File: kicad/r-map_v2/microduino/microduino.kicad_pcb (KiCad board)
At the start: 2 copper layers, 25.4 x 29.2 mm, 15 parts, among them P1 CONN_01X02, P2 CONN_RELE_BOARD, P3 CONN_01X05, P4 CONFIG, P5 USB, U1 Microduino, U2 ESDA6V1-5SC6, U3 LP2985LV, U4 TMP275

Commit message: Add files from last commit on sourceforge
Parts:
- removed R1: 1K0, w_smd_resistors:r_1206
- D1: value LED -> LED_SMD
- P5: value USB -> USB_OTG
- R2: value R -> 150
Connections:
- net Net-(C1-Pad1) renamed /+5V
- net Net-(C3-Pad1) renamed /+3.3V
- net Net-(P3-Pad2) renamed /SCL
- net Net-(P3-Pad3) renamed /SDA
- U4 pad 5: Net-(R1-Pad1) -> GND
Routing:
- net GND: track 93.1 -> 105.6 mm
- net Net-(R1-Pad1): track 11.2 -> 0.00 mm
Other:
- board text added: "+5V"
- board text added: "-"
- board text added: "3.3V"
- board text added: "GND"
- board text added: "REL1"
- board text added: "REL2"
- board text added: "REL3"
- board text added: "REL4"
- board text added: "SCL"
- board text added: "SDA"
- board text added: "SET"

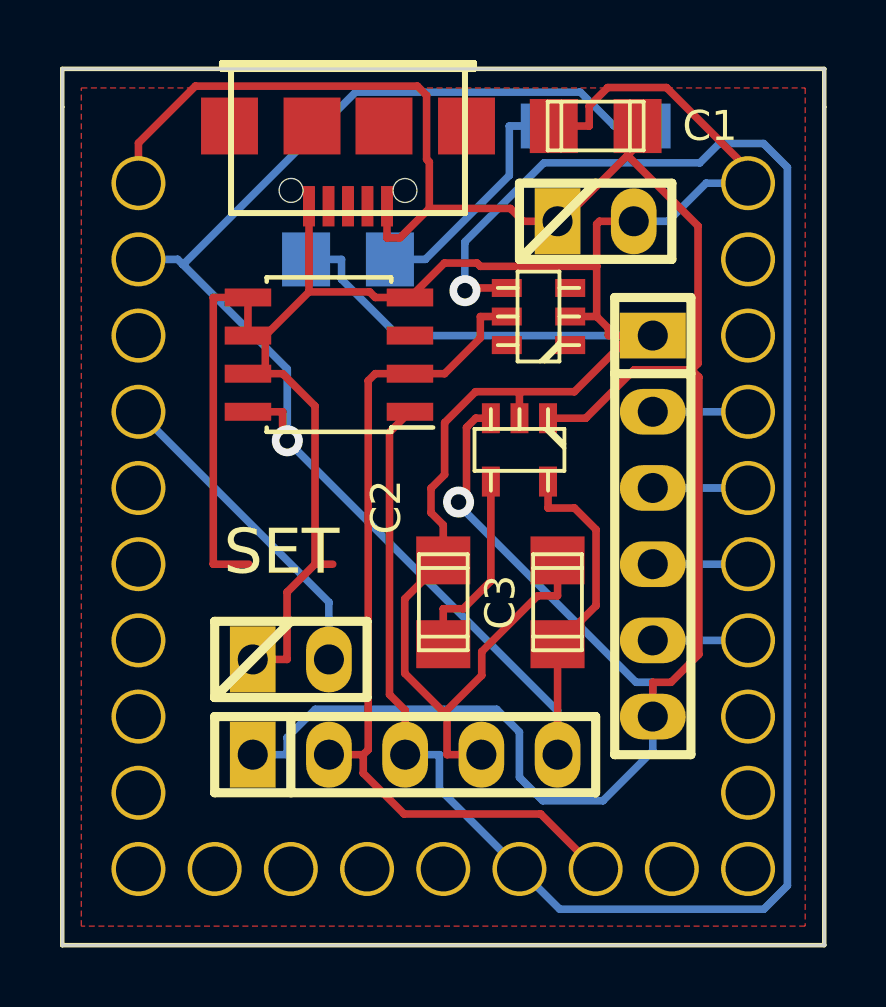
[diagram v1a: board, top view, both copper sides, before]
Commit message: Modifiche a schema elettrico su modulo bluethoot, modificate connessioni per seriale 1. Modulo stima-i2c modificati pin per rele' e aggiunte connessioni esd su alimentazione. Rigenerati pcb.
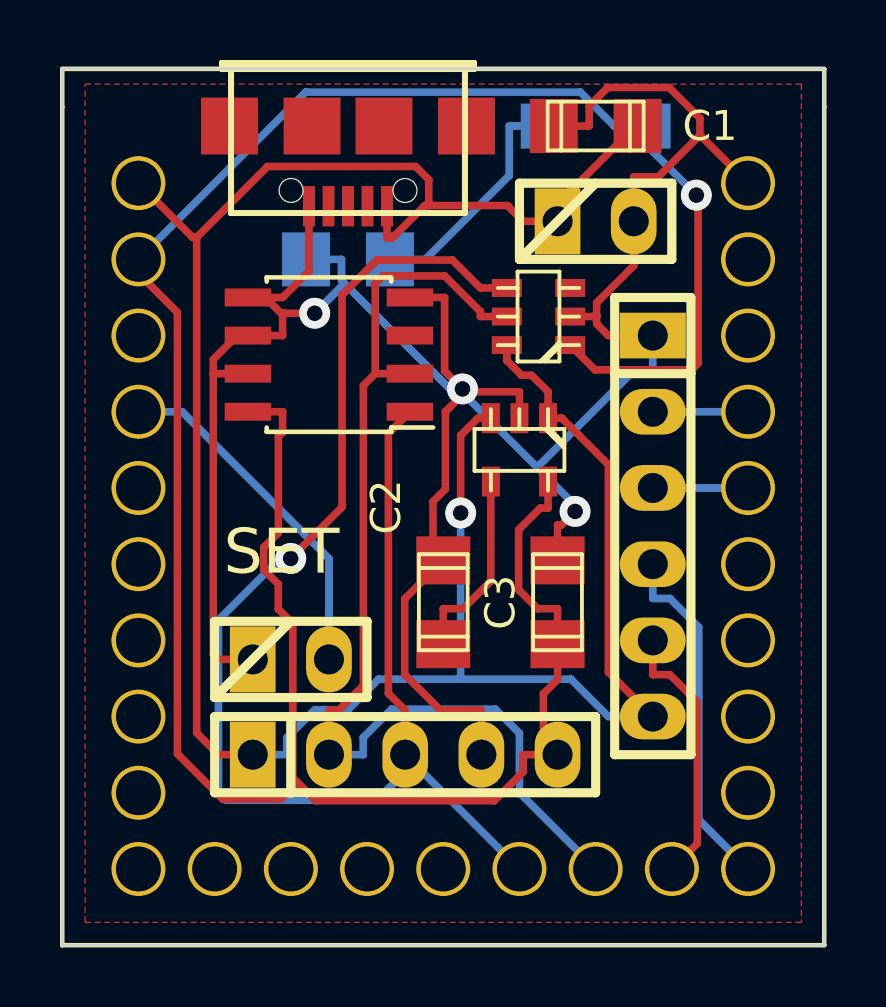
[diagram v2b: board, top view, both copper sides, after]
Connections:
- P5 pad 2: (no net) -> Net-(P5-Pad2)
- P5 pad 3: (no net) -> Net-(P5-Pad3)
- P5 pad 4: (no net) -> Net-(P5-Pad4)
- U1 pad 10: (no net) -> Net-(P2-Pad4)
- U1 pad 11: (no net) -> Net-(P2-Pad5)
- U1 pad 14: (no net) -> Net-(U1-Pad14)
- U1 pad 15: (no net) -> Net-(U1-Pad15)
- U1 pad 16: (no net) -> Net-(U1-Pad16)
- U1 pad 17: (no net) -> Net-(U1-Pad17)
- U1 pad 18: (no net) -> Net-(U1-Pad18)
- U1 pad 19: (no net) -> Net-(U1-Pad19)
- U1 pad 2: (no net) -> Net-(U1-Pad2)
- U1 pad 20: (no net) -> Net-(U1-Pad20)
- U1 pad 21: (no net) -> Net-(U1-Pad21)
- U1 pad 22: (no net) -> Net-(U1-Pad22)
- U1 pad 23: (no net) -> Net-(U1-Pad23)
- U1 pad 25: (no net) -> Net-(U1-Pad25)
- U1 pad 3: (no net) -> Net-(U1-Pad3)
- U1 pad 6: Net-(P2-Pad4) -> Net-(U1-Pad6)
- U1 pad 7: Net-(P2-Pad5) -> Net-(U1-Pad7)
- U1 pad 8: (no net) -> Net-(U1-Pad8)
- U1 pad 9: (no net) -> Net-(U1-Pad9)
- U2 pad 1: (no net) -> /+3.3V
- U2 pad 3: (no net) -> Net-(U2-Pad3)
- U2 pad 6: (no net) -> /+5V
- U4 pad 3: (no net) -> Net-(U4-Pad3)
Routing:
- net /+3.3V: track 54.4 -> 90.1 mm
- net GND: track 105.6 -> 87.4 mm, vias 0 -> 3
- net /SDA: track 67.2 -> 49.3 mm
- net Net-(P2-Pad4): track 3.18 -> 11.8 mm
- net /SCL: track 29.3 -> 36.1 mm
- net Net-(P2-Pad5): track 3.18 -> 8.92 mm
- net /+5V: track 85.6 -> 82.6 mm
- net Net-(P4-Pad2): track 10.9 -> 11.7 mm

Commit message: Aggiunto ponticello a saldare per uscita 3.3V. Nuovo design per i2chub
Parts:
- added P6: CONN_01X01, Measurement_Points:Measurement_Point_Square-SMD-Pad_Small, B.Cu at (144.8, 104.1)
- added P7: CONN_01X01, Measurement_Points:Measurement_Point_Square-SMD-Pad_Small, B.Cu at (142.2, 104.1)
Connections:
- U3 pad 5: /+3.3V -> Net-(P6-Pad1)
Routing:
- net /+3.3V: track 90.1 -> 62.2 mm, vias 1 -> 2
- net /SDA: track 49.3 -> 24.0 mm, vias 1 -> 0
- net /SCL: track 36.1 -> 47.3 mm, vias 0 -> 1
- net /+5V: track 82.6 -> 93.3 mm
- net Net-(P6-Pad1): track 0.00 -> 8.43 mm, vias 0 -> 1
- net GND: track 87.4 -> 88.7 mm, vias 3 -> 1

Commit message: Sistemato orientamento case led smd, generati files gbr per i2c hub e breakout board
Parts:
- turned D1 to 180 degrees
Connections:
- D1 pad 1: Net-(D1-Pad1) -> /+3.3V
- D1 pad 2: /+3.3V -> Net-(D1-Pad2)
- P5 pad 2: Net-(P5-Pad2) -> (no net)
- P5 pad 3: Net-(P5-Pad3) -> (no net)
- P5 pad 4: Net-(P5-Pad4) -> (no net)
- R2 pad 1: Net-(D1-Pad1) -> Net-(D1-Pad2)
- U1 pad 14: Net-(U1-Pad14) -> (no net)
- U1 pad 15: Net-(U1-Pad15) -> (no net)
- U1 pad 16: Net-(U1-Pad16) -> (no net)
- U1 pad 17: Net-(U1-Pad17) -> (no net)
- U1 pad 18: Net-(U1-Pad18) -> (no net)
- U1 pad 19: Net-(U1-Pad19) -> (no net)
- U1 pad 2: Net-(U1-Pad2) -> (no net)
- U1 pad 20: Net-(U1-Pad20) -> (no net)
- U1 pad 21: Net-(U1-Pad21) -> (no net)
- U1 pad 22: Net-(U1-Pad22) -> (no net)
- U1 pad 23: Net-(U1-Pad23) -> (no net)
- U1 pad 25: Net-(U1-Pad25) -> (no net)
- U1 pad 3: Net-(U1-Pad3) -> (no net)
- U1 pad 6: Net-(U1-Pad6) -> (no net)
- U1 pad 7: Net-(U1-Pad7) -> (no net)
- U1 pad 8: Net-(U1-Pad8) -> (no net)
- U1 pad 9: Net-(U1-Pad9) -> (no net)
- U2 pad 3: Net-(U2-Pad3) -> (no net)
- U4 pad 3: Net-(U4-Pad3) -> (no net)
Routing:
- net Net-(D1-Pad2): track 0.00 -> 7.92 mm
- net Net-(D1-Pad1): track 7.92 -> 0.00 mm

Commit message: Aggiornamento lista componenti e cancellazione vecchi files
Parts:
- U3: value LP2985LV -> REG113NA-3.3/250
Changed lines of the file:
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@@
-(kicad_pcb (version 4) (host pcbnew 0.201509251832+6217~30~ubuntu14.04.1-product)
+(kicad_pcb (version 4) (host pcbnew 0.201510090346+6256~30~ubuntu14.04.1-product)
   (general
     (links 43)
     (no_connects 0)
-    (area 135.560999 88.350089 177.545 118.439001)
+    (area 135.560999 88.350089 161.619001 118.439001)
     (thickness 1.6)
     (drawings 21)
@@
       (effects (font (size 1 1) (thickness 0.2)))
     )
-    (fp_text value LP2985LV (at 0 0 180) (layer F.SilkS) hide
+    (fp_text value REG113NA-3.3/250 (at 0 0 180) (layer F.SilkS) hide
       (effects (font (size 0.50038 0.50038) (thickness 0.09906)))
     )

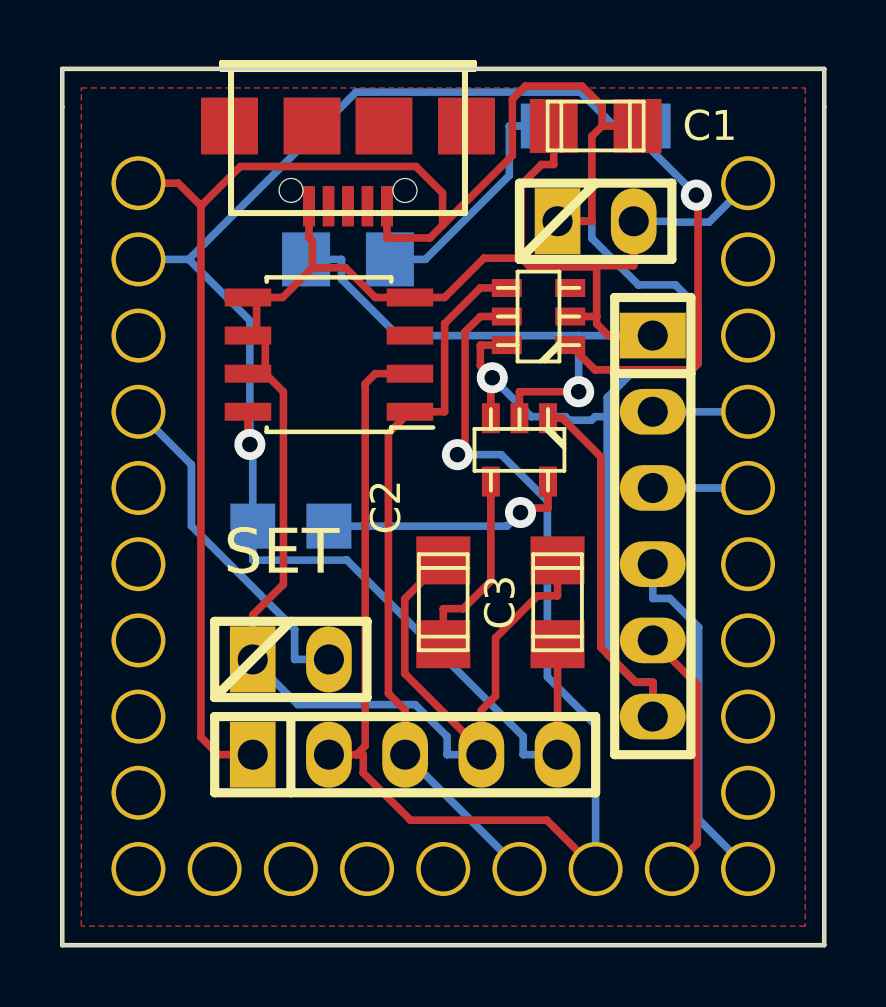
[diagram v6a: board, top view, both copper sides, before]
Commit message: Nouva versione pcb, doppia schermatura, allargamento piste, rimozione connessioni T ed Y
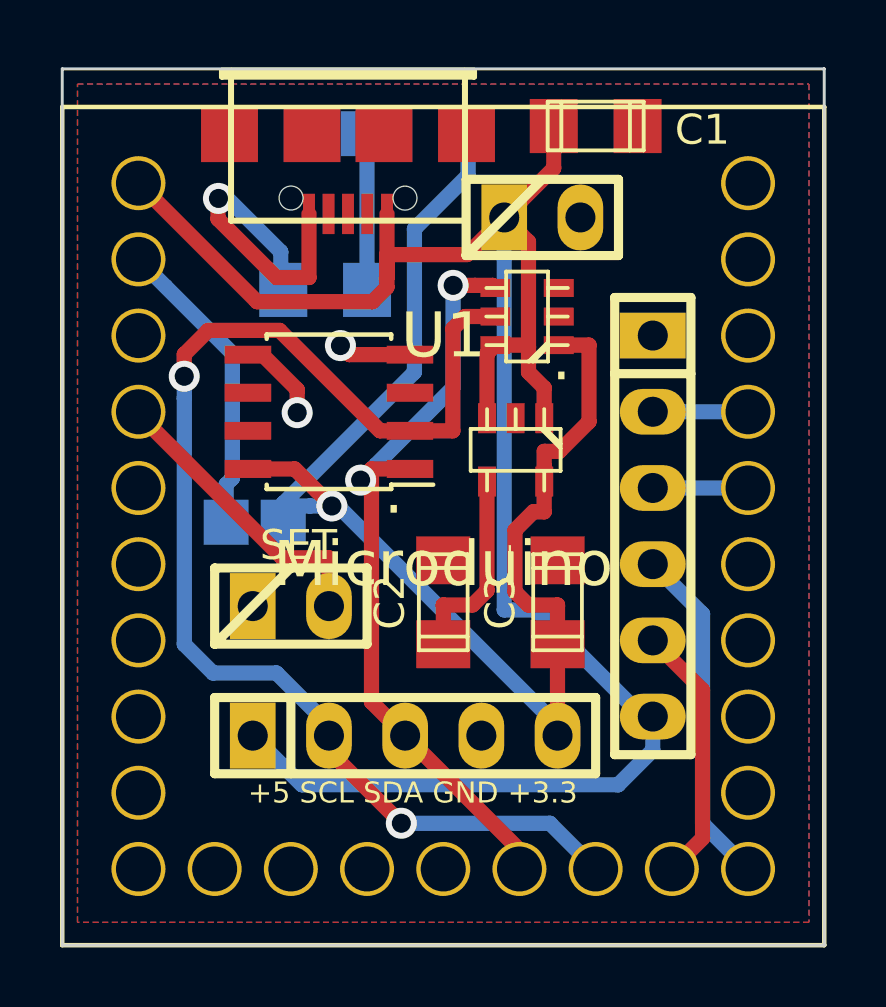
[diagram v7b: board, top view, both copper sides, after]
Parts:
- R2: value 150 -> 820
- moved D1 6.00 mm to (147.7, 91.1), turned to 0 degrees
- moved P6 3.43 mm to (141.4, 104.0)
- moved U4 1.91 mm to (144.8, 100.3)
- moved P1 1.78 mm to (151.9, 93.9)
- moved P4 1.78 mm to (143.5, 106.8)
- moved R2 1.27 mm to (144.7, 96.3)
- moved P7 1.02 mm to (143.3, 104.0)
- moved P3 0.64 mm to (147.3, 111.1)
- moved U2 0.38 mm to (151.4, 97.2)
- moved P5 0.25 mm to (145.4, 91.1)
- moved U3 0.13 mm to (151.0, 101.6)
- turned C1 to 180 degrees
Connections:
- D1 pad 1: /+3.3V -> Net-(D1-Pad1)
- D1 pad 2: Net-(D1-Pad2) -> /+3.3V
- R2 pad 1: Net-(D1-Pad2) -> Net-(D1-Pad1)
- U1 pad 26: /+3.3V -> Net-(P6-Pad1)
- U3 pad 5: Net-(P6-Pad1) -> /+3.3V
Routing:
- net GND: track 88.7 -> 15.9 mm, vias 1 -> 3
- net /+5V: track 93.3 -> 67.6 mm, vias 1 -> 0
- net /+3.3V: track 62.2 -> 48.1 mm, vias 2 -> 1
- net Net-(D1-Pad2): track 7.92 -> 0.00 mm
- net Net-(D1-Pad1): track 0.00 -> 5.26 mm
- net /SCL: track 47.3 -> 42.6 mm, vias 1 -> 2
- net /SDA: track 24.0 -> 26.4 mm, vias 0 -> 2
- net Net-(P6-Pad1): track 8.43 -> 10.1 mm, vias 1 -> 0
- net Net-(P4-Pad2): track 11.6 -> 10.0 mm
- added copper zone on B.Cu, net GND
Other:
- net class Futura added: clearance 0.254, trace_width 0.508, via_dia 1.035, via_drill 0.635
- board text added: "+3.3 GND SDA SCL +5"
- board text added: "+5"
- board text added: "+5 SCL SDA GND +3.3"
- board text added: "+5.5"
- board text added: "."
- board text added: "GND RL1 RL2 RL3 RL4"
- board text removed: "+5V"
- board text removed: "3.3V"
- board text removed: "REL1"
- board text removed: "REL2"
- board text removed: "REL3"
- board text removed: "REL4"
- board text removed: "SCL"
- board text removed: "SDA"
